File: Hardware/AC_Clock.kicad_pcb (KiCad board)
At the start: 0 parts

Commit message: Set Footprints for components
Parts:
- added C1: 10u, Capacitor_SMD:C_0603_1608Metric, F.Cu at (223.5, 124.5)
- added C2: 22u, Capacitor_SMD:C_0603_1608Metric, F.Cu at (223.5, 127.0)
- added C3: 0.1u, Capacitor_SMD:C_0603_1608Metric, F.Cu at (223.5, 129.5)
- added C4: 0.1u, Capacitor_SMD:C_0603_1608Metric, F.Cu at (223.5, 132.1)
- added C5: 0.1u, Capacitor_SMD:C_0603_1608Metric, F.Cu at (223.5, 134.6)
- added C6: 0.1u, Capacitor_SMD:C_0603_1608Metric, F.Cu at (172.8, 56.0)
- added C7: 0.1u, Capacitor_SMD:C_0603_1608Metric, F.Cu at (172.8, 58.5)
- added C8: 0.1u, Capacitor_SMD:C_0603_1608Metric, F.Cu at (172.8, 61.0)
- added C9: 0.1u, Capacitor_SMD:C_0603_1608Metric, F.Cu at (172.8, 63.5)
- added D1: ABS2, Diode_SMD:Diode_Bridge_Diotec_ABS, F.Cu at (87.6, 124.5)
- added D10: 1N4148WT, Diode_SMD:D_SOD-523, F.Cu at (216.2, 129.4)
- added D11: 1N4148WT, Diode_SMD:D_SOD-523, F.Cu at (216.2, 131.8)
- added D12: 1N4148WT, Diode_SMD:D_SOD-523, F.Cu at (216.2, 134.3)
- added D13: 1N4148WT, Diode_SMD:D_SOD-523, F.Cu at (216.2, 136.7)
- added D14: 1N4148WT, Diode_SMD:D_SOD-523, F.Cu at (219.7, 124.5)
- added D15: 1N4148WT, Diode_SMD:D_SOD-523, F.Cu at (219.7, 126.9)
- added D16: 1N4148WT, Diode_SMD:D_SOD-523, F.Cu at (219.7, 129.4)
- added D17: 1N4148WT, Diode_SMD:D_SOD-523, F.Cu at (219.7, 131.8)
- added D18: 1N4148WT, Diode_SMD:D_SOD-523, F.Cu at (219.7, 134.3)
- added D2: 1N4148WT, Diode_SMD:D_SOD-523, F.Cu at (212.6, 124.5)
- added D3: 1N4148WT, Diode_SMD:D_SOD-523, F.Cu at (212.6, 126.9)
- added D4: 1N4148WT, Diode_SMD:D_SOD-523, F.Cu at (212.6, 129.4)
- added D5: 1N4148WT, Diode_SMD:D_SOD-523, F.Cu at (212.6, 131.8)
- added D6: 1N4148WT, Diode_SMD:D_SOD-523, F.Cu at (212.6, 134.3)
- added D7: 1N4148WT, Diode_SMD:D_SOD-523, F.Cu at (212.6, 136.7)
- added D8: 1N4148WT, Diode_SMD:D_SOD-523, F.Cu at (216.2, 124.5)
- added D9: 1N4148WT, Diode_SMD:D_SOD-523, F.Cu at (216.2, 126.9)
- added F1: LVR005NS, Fuse:Fuse_BelFuse_0ZRE0005FF_L8.3mm_W3.8mm, F.Cu at (38.9, 119.3)
- added J1: L, JKC_Library:Keystone_1287, F.Cu at (38.1, 113.0)
- added J2: N, JKC_Library:Keystone_1287, F.Cu at (38.1, 141.0)
- added JP1: Freq Sel., Jumper:SolderJumper-3_P1.3mm_Bridged12_RoundedPad1.0x1.5mm, F.Cu at (213.6, 139.7)
- added R1: 1k, Resistor_SMD:R_0805_2012Metric, F.Cu at (87.6, 119.5)
- added R10: 1k, Resistor_SMD:R_0805_2012Metric, F.Cu at (221.5, 111.2)
- added R2: 1k, Resistor_SMD:R_0805_2012Metric, F.Cu at (212.6, 105.3)
- added R3: 1k, Resistor_SMD:R_0805_2012Metric, F.Cu at (212.6, 108.3)
- added R4: 1k, Resistor_SMD:R_0805_2012Metric, F.Cu at (212.6, 111.2)
- added R5: 1k, Resistor_SMD:R_0805_2012Metric, F.Cu at (217.1, 105.3)
- added R6: 1k, Resistor_SMD:R_0805_2012Metric, F.Cu at (217.1, 108.3)
- added R7: 1k, Resistor_SMD:R_0805_2012Metric, F.Cu at (217.1, 111.2)
- added R8: 1k, Resistor_SMD:R_0805_2012Metric, F.Cu at (221.5, 105.3)
- added R9: 1k, Resistor_SMD:R_0805_2012Metric, F.Cu at (221.5, 108.3)
- added RN1: 1k, Resistor_SMD:R_Array_Convex_4x0603, F.Cu at (172.9, 47.6)
- added RN2: 1k, Resistor_SMD:R_Array_Convex_4x0603, F.Cu at (177.0, 47.6)
- added RN3: 1k, Resistor_SMD:R_Array_Convex_4x0603, F.Cu at (181.2, 47.6)
- added RN4: 1k, Resistor_SMD:R_Array_Convex_4x0603, F.Cu at (185.3, 47.6)
- added RN5: 1k, Resistor_SMD:R_Array_Convex_4x0603, F.Cu at (189.5, 47.6)
- added RN6: 1k, Resistor_SMD:R_Array_Convex_4x0603, F.Cu at (172.9, 52.4)
- added RN7: 1k, Resistor_SMD:R_Array_Convex_4x0603, F.Cu at (177.0, 52.4)
- added RN8: 1k, Resistor_SMD:R_Array_Convex_4x0603, F.Cu at (181.2, 52.4)
- added RV1: V180ZA, Varistor:RV_Disc_D7mm_W5.1mm_P5mm, F.Cu at (36.9, 134.7)
- added SW1: SW_Push, Button_Switch_SMD:SW_SPST_PTS645, F.Cu at (194.3, 127.2)
- added SW2: SW_Push, Button_Switch_SMD:SW_SPST_PTS645, F.Cu at (194.3, 135.0)
- added T1: 10:1, JKC_Library:Transformer_CL2-5.0R-12, F.Cu at (63.5, 127.0)
- added U1: AZ1117-5.0, Package_TO_SOT_SMD:SOT-223-3_TabPin2, F.Cu at (215.4, 116.9)
- added U10: 4511, Package_SO:TSSOP-16_4.4x5mm_P0.65mm, F.Cu at (166.4, 61.7)
- added U11: HDSP-816E, JKC_Library:Broadcom_HDSP-81x, F.Cu at (216.4, 30.5)
- added U12: 4511, Package_SO:TSSOP-16_4.4x5mm_P0.65mm, F.Cu at (166.4, 68.3)
- added U13: HDSP-816E, JKC_Library:Broadcom_HDSP-81x, F.Cu at (238.2, 30.5)
- added U2: LTV-817S, Package_DIP:SMDIP-6_W9.53mm_Clearance8mm, F.Cu at (90.2, 113.0)
- added U3: 4040, Package_DIP:DIP-16_W7.62mm, F.Cu at (106.7, 119.4)
- added U4: 74LS393, Package_DIP:DIP-14_W7.62mm, F.Cu at (121.9, 130.8)
- added U5: 74LS393, Package_DIP:DIP-14_W7.62mm, F.Cu at (147.3, 130.8)
- added U6: 4511, Package_SO:TSSOP-16_4.4x5mm_P0.65mm, F.Cu at (166.4, 48.5)
- added U7: HDSP-816E, JKC_Library:Broadcom_HDSP-81x, F.Cu at (172.7, 30.5)
- added U8: 4511, Package_SO:TSSOP-16_4.4x5mm_P0.65mm, F.Cu at (166.4, 55.1)
- added U9: HDSP-816E, JKC_Library:Broadcom_HDSP-81x, F.Cu at (194.5, 30.5)
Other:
- copper layers 0 -> 2

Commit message: Work on routing
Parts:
- removed D12: 1N4148WT, Diode_SMD:D_SOD-523
- removed R8: 1k, Resistor_SMD:R_0805_2012Metric
- R1, R10, R2, R3, R4, R5, R6, R7, R9: footprint Resistor_SMD:R_0805_2012Metric -> Resistor_SMD:R_0603_1608Metric
- SW1: value SW_Push -> Min_PB
- SW2: value SW_Push -> Hr_PB
- U11, U13, U7, U9: moved to B.Cu
- moved C1 137.9 mm to (85.9, 132.1)
- moved C2 133.9 mm to (89.7, 132.1)
- moved U1 129.5 mm to (87.6, 138.4), turned to -90 degrees
- moved C3 126.1 mm to (97.8, 139.7), turned to -90 degrees
- moved R2 119.5 mm to (94.0, 119.8), turned to 90 degrees
- moved R3 117.5 mm to (95.2, 113.0), turned to -90 degrees
- moved D4 115.9 mm to (97.8, 113.0), turned to 90 degrees
- moved C4 113.3 mm to (110.5, 124.5), turned to -90 degrees
- moved D3 113.1 mm to (100.3, 113.0), turned to 90 degrees
- moved D2 110.3 mm to (102.9, 113.0), turned to 90 degrees
- moved D5 108.8 mm to (105.4, 113.0), turned to 90 degrees
- moved JP1 105.6 mm to (108.0, 142.2), turned to 180 degrees
- moved D15 104.5 mm to (115.6, 134.6), turned to -90 degrees
- moved R9 104.2 mm to (120.7, 134.6), turned to 90 degrees
- moved D16 101.8 mm to (118.1, 134.6), turned to -90 degrees
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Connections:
- net Net-(D16-A) renamed /SetM
- net Net-(D18-A) renamed /SetH
- net Net-(D3-K) renamed /16s
- net Net-(D4-K) renamed /8s
- net Net-(F1-Pad2) renamed /Fused
- D14 pad 2: /RST_{10hr} -> DA_4
- D2 pad 1: /minute -> /32s
- D2 pad 2: Net-(D2-A) -> /minute
- D3 pad 2: Net-(D2-A) -> /minute
- D4 pad 2: Net-(D2-A) -> /minute
- D5 pad 2: Net-(D2-A) -> /minute
- R3 pad 1: Net-(D2-A) -> /minute
- U3 pad 1: /minute -> /32s
- U3 pad 11: Net-(D2-A) -> /minute
- U5 pad 12: /RST_{10hr} -> DA_4
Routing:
- net +5V: track 0.00 -> 143.3 mm, vias 0 -> 2
- net /AC_12+: track 0.00 -> 50.8 mm
- net Earth: track 0.00 -> 50.4 mm
- net /minute: track 0.00 -> 45.7 mm, vias 0 -> 1
- net Net-(JP1-C): track 0.00 -> 41.8 mm
- net /Fused: track 0.00 -> 40.0 mm
- net /10hr: track 0.00 -> 27.7 mm
- net GND: track 0.00 -> 24.9 mm, vias 0 -> 10
- net /32s: track 0.00 -> 23.2 mm
- net /10m: track 0.00 -> 22.7 mm
- net /16s: track 0.00 -> 20.7 mm
- net /8s: track 0.00 -> 18.5 mm
- net AC: track 0.00 -> 17.2 mm
- net /AC_12-: track 0.00 -> 14.7 mm
- net DA_4: track 0.00 -> 14.2 mm
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- added copper zone on B.Cu, net Earth
- added copper zone on B.Cu, net GND
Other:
- board outline added: 127 x 40.6 mm

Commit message: Add in correct calculated times for frequency divider
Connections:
- net /16s renamed /17s
- net /32s renamed /34s
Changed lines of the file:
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@@
 	(net 111 "unconnected-(RN8-R4.1-Pad4)")
 	(net 112 "unconnected-(RN8-R4.2-Pad5)")
-	(net 113 "/32s")
-	(net 114 "/16s")
+	(net 113 "/34s")
+	(net 114 "/17s")
 	(net 115 "/8s")
 	(net 116 "/Fused")
@@
 			(layers "F.Cu" "F.Paste" "F.Mask")
 			(roundrect_rratio 0.25)
-			(net 114 "/16s")
+			(net 114 "/17s")
 			(pinfunction "K")
 			(pintype "passive")
@@
 			(layers "F.Cu" "F.Paste" "F.Mask")
 			(roundrect_rratio 0.25)
-			(net 113 "/32s")
+			(net 113 "/34s")
 			(pinfunction "K")
 			(pintype "passive")
@@
 		)
 		(fp_text user "${REFERENCE}"
-			(at 0 0 360)
+			(at 0 0 0)
 			(layer "F.Fab")
 			(effects
@@
 		(tags "net tie solder jumper bridged")
 		(property "Reference" "JP1"
-			(at 0 -1.8 360)
+			(at 0 -1.8 0)
 			(layer "F.SilkS")
 			(effects
@@
 		)
 		(property "Value" "Freq Sel."
-			(at 0 1.9 360)
+			(at 0 1.9 0)
 			(layer "F.Fab")
 			(effects
@@
 		(tags "SPST Button Switch")
 		(property "Reference" "SW2"
-			(at 0 -4.05 360)
+			(at 0 -4.05 0)
 			(layer "F.SilkS")
 			(hide yes)
@@
 		)
 		(property "Value" "Hr_PB"
-			(at 0 -5.08 360)
+			(at 0 -5.08 0)
 			(layer "F.SilkS")
 			(effects
@@
 		)
 		(fp_text user "${REFERENCE}"
-			(at 0 -4.05 360)
+			(at 0 -4.05 0)
 			(layer "F.Fab")
 			(effects
@@
 		(tags "SPST Button Switch")
 		(property "Reference" "SW1"
-			(at 0 -4.05 360)
+			(at 0 -4.05 0)
 			(layer "F.SilkS")
 			(hide yes)
@@
 		)
 		(property "Value" "Min_PB"
-			(at 0 -5.08 360)
+			(at 0 -5.08 0)
 			(layer "F.SilkS")
 			(effects
@@
 		)
 		(fp_text user "${REFERENCE}"
-			(at 0 -4.05 360)
+			(at 0 -4.05 0)
 			(layer "F.Fab")
 			(effects
@@
 		(tags "THT DIP DIL PDIP 2.54mm 7.62mm 300mil")
 		(property "Reference" "U3"
-			(at 3.81 -2.33 360)
+			(at 3.81 -2.33 0)
 			(layer "F.SilkS")
 			(effects
@@
 		)
 		(property "Value" "4040"
-			(at 3.81 20.11 360)
+			(at 3.81 20.11 0)
 			(layer "F.Fab")
 			(effects
@@
 		)
 		(fp_text user "${REFERENCE}"
-			(at 3.81 8.89 360)
+			(at 3.81 8.89 0)
 			(layer "F.Fab")
 			(effects
@@
 			(layers "*.Cu" "*.Mask")
 			(remove_unused_layers no)
-			(net 113 "/32s")
+			(net 113 "/34s")
 			(pinfunction "Q11")
 			(pintype "output")
@@
 			(layers "*.Cu" "*.Mask")
 			(remove_unused_layers no)
-			(net 114 "/16s")
+			(net 114 "/17s")
 			(pinfunction "Q10")
 			(pintype "output")
@@
 		)
 		(fp_text user "${REFERENCE}"
-			(at -1.27 -11.43 360)
+			(at -1.27 -11.43 0)
 			(layer "B.Fab")
 			(effects
@@
 		)
 		(fp_text user "${REFERENCE}"
-			(at -1.27 -11.43 360)
+			(at -1.27 -11.43 0)
 			(layer "B.Fab")
 			(effects
@@
 		)
 		(fp_text user "${REFERENCE}"
-			(at -1.27 -11.43 360)
+			(at -1.27 -11.43 0)
 			(layer "B.Fab")
 			(effects
@@
 		)
 		(fp_text user "${REFERENCE}"
-			(at -1.27 -11.43 360)
+			(at -1.27 -11.43 0)
 			(layer "B.Fab")
 			(effects

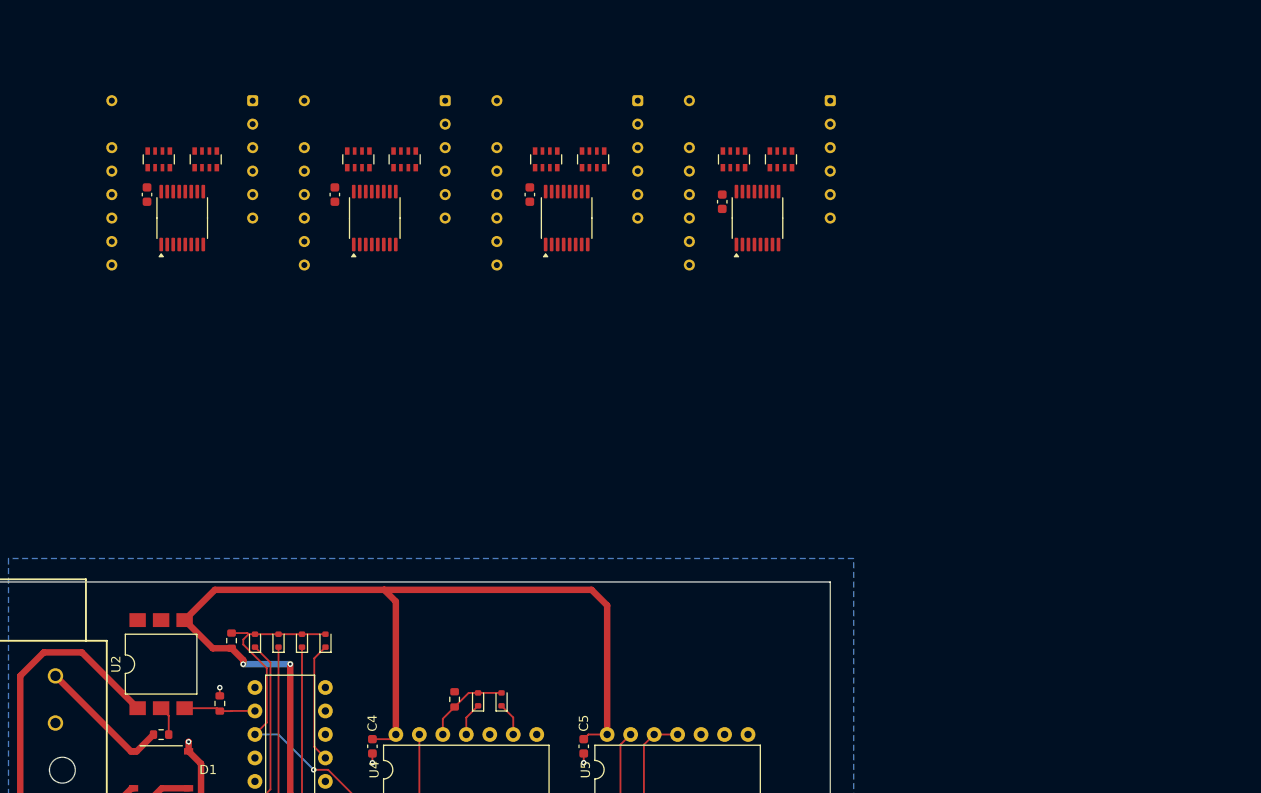
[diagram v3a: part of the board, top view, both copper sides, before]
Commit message: Add in connectors for display board interconnect
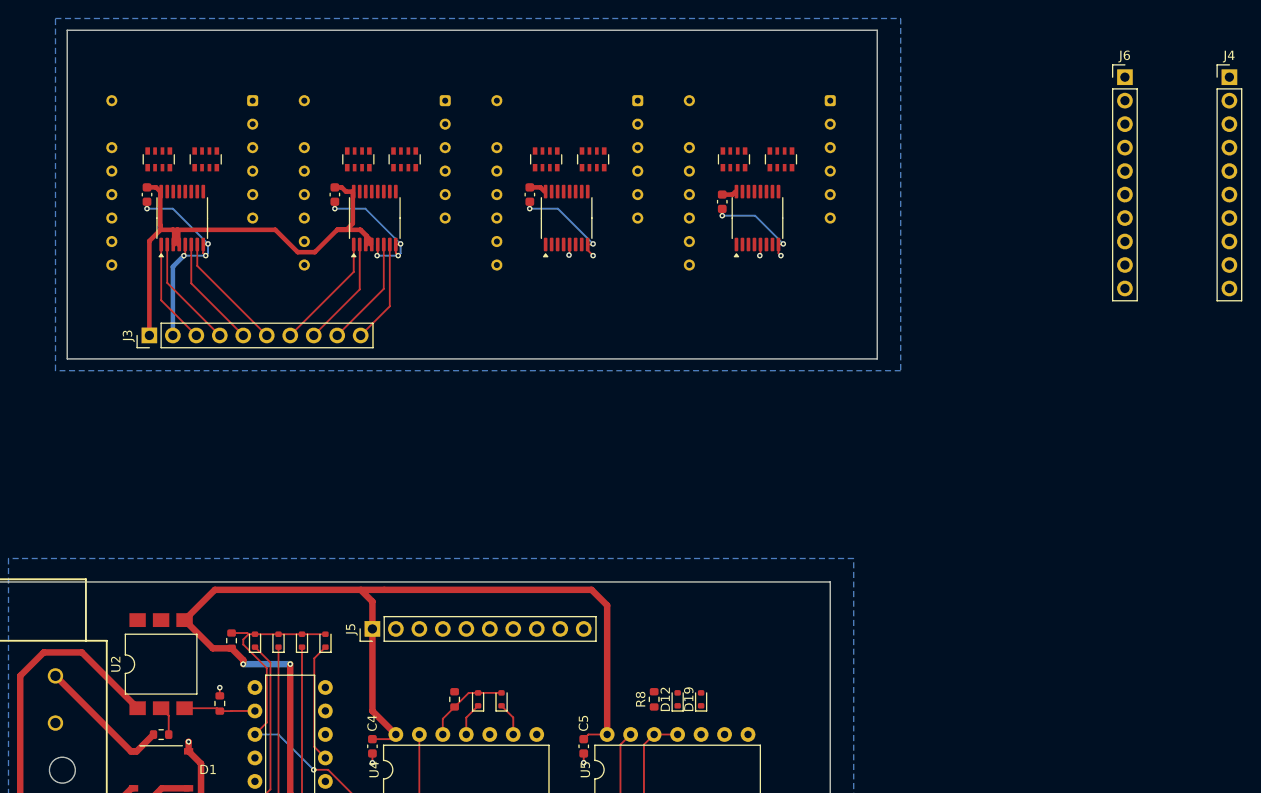
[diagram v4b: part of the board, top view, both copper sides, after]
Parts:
- added D12: 1N4148WT, Diode_SMD:D_SOD-523, F.Cu at (143.5, 119.4)
- added D19: 1N4148WT, Diode_SMD:D_SOD-523, F.Cu at (146.1, 119.4)
- added J3: Conn_01x10, Connector_PinHeader_2.54mm:PinHeader_1x10_P2.54mm_Vertical, F.Cu at (86.4, 80.0)
- added J4: Conn_01x10, Connector_PinHeader_2.54mm:PinHeader_1x10_P2.54mm_Vertical, F.Cu at (203.2, 52.1)
- added J5: Conn_01x10, Connector_PinHeader_2.54mm:PinHeader_1x10_P2.54mm_Vertical, F.Cu at (110.5, 111.8)
- added J6: Conn_01x10, Connector_PinHeader_2.54mm:PinHeader_1x10_P2.54mm_Vertical, F.Cu at (191.9, 52.1)
- added R8: 1k, Resistor_SMD:R_0603_1608Metric, F.Cu at (141.0, 119.4)
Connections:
- D11 pad 1: DA_3 -> DB_3
- D14 pad 2: DA_4 -> /RST_{10hr}
- D7 pad 1: DA_1 -> DB_1
- D9 pad 1: DA_2 -> DB_2
- U5 pad 12: DA_4 -> /RST_{10hr}
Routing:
- net GND: track 24.9 -> 90.1 mm, vias 10 -> 26
- net +5V: track 143.3 -> 203.8 mm
- net DA_1: track 6.38 -> 19.3 mm
- net DB_2: track 0.00 -> 12.7 mm
- net DC_1: track 0.00 -> 12.2 mm
- net DD_1: track 3.12 -> 15.3 mm
- net DD_2: track 0.00 -> 11.9 mm
- net DC_2: track 3.62 -> 15.5 mm
- net DB_1: track 0.00 -> 11.4 mm
- net DA_2: track 3.63 -> 14.8 mm
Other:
- board size 127 x 40.6 mm -> 132.1 x 100.3 mm

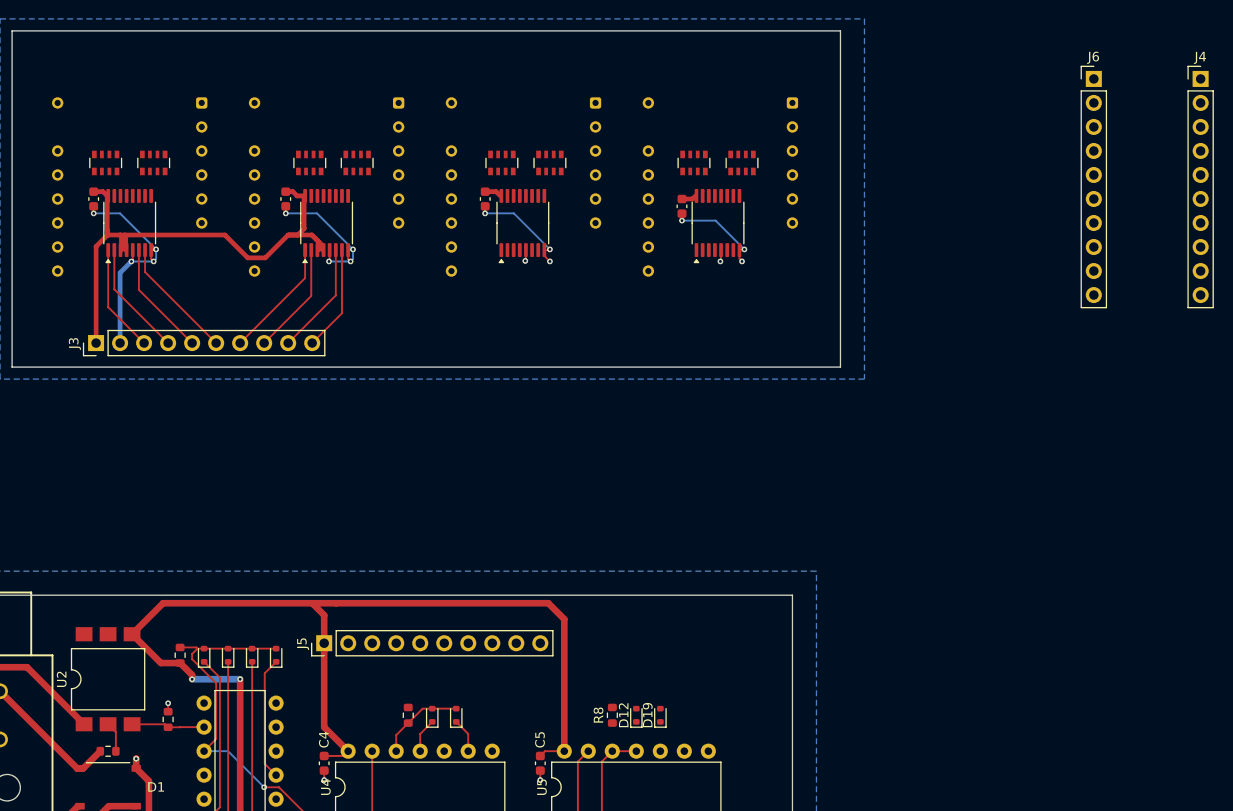
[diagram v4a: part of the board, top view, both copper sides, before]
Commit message: Adjust minutes resistor packs to make them flow better
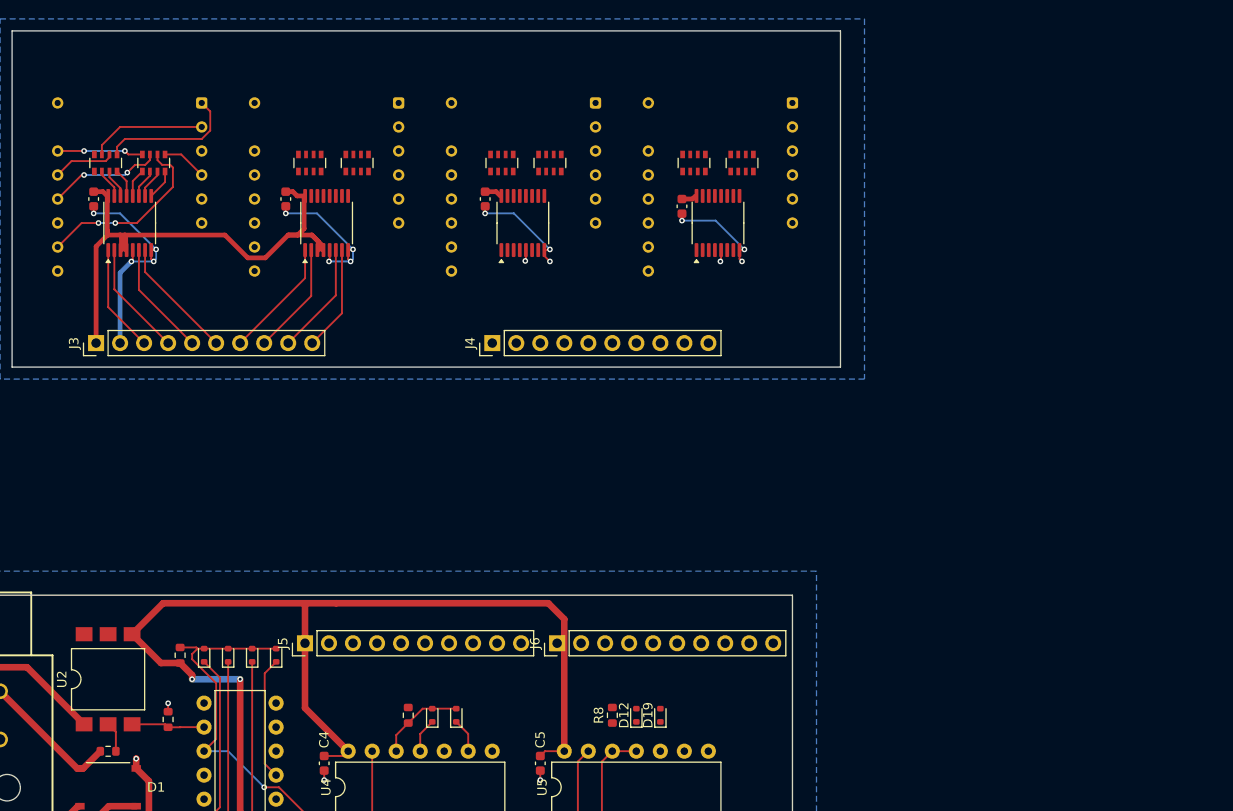
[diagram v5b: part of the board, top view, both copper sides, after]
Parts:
- moved J6 82.4 mm to (135.1, 111.8), turned to 90 degrees
- moved J4 80.0 mm to (128.3, 80.0), turned to 90 degrees
- moved J5 2.03 mm to (108.5, 111.8)
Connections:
- RN2 pad 1: Net-(RN2-R1.1) -> unconnected-(RN2A-R1.1-Pad1)
- RN2 pad 4: unconnected-(RN2-R4.1-Pad4) -> Net-(RN2D-R4.1)
- RN2 pad 5: unconnected-(RN2-R4.2-Pad5) -> Net-(RN2D-R4.2)
- RN2 pad 8: Net-(RN2-R1.2) -> unconnected-(RN2A-R1.2-Pad8)
- RN3 pad 1: Net-(RN3-R1.1) -> unconnected-(RN3A-R1.1-Pad1)
- RN3 pad 2: Net-(RN3-R2.1) -> Net-(RN3B-R2.1)
- RN3 pad 3: Net-(RN3-R3.1) -> Net-(RN3C-R3.1)
- RN3 pad 4: Net-(RN3-R4.1) -> Net-(RN3D-R4.1)
- RN3 pad 5: Net-(RN3-R4.2) -> Net-(RN3D-R4.2)
- RN3 pad 6: Net-(RN3-R3.2) -> Net-(RN3C-R3.2)
- RN3 pad 7: Net-(RN3-R2.2) -> Net-(RN3B-R2.2)
- RN3 pad 8: Net-(RN3-R1.2) -> unconnected-(RN3A-R1.2-Pad8)
- RN4 pad 4: unconnected-(RN4-R4.1-Pad4) -> Net-(RN4-R4.1)
- RN4 pad 5: unconnected-(RN4-R4.2-Pad5) -> Net-(RN4-R4.2)
- U6 pad 10: Net-(RN1-R4.1) -> Net-(RN1-R3.1)
- U6 pad 11: Net-(RN1-R3.1) -> Net-(RN1-R2.1)
- U6 pad 12: Net-(RN1-R2.1) -> Net-(RN1-R1.1)
- U6 pad 13: Net-(RN1-R1.1) -> Net-(RN2D-R4.1)
- U6 pad 9: Net-(RN2-R1.1) -> Net-(RN1-R4.1)
- U7 pad 1: Net-(RN1-R1.2) -> Net-(RN2D-R4.2)
- U7 pad 10: Net-(RN1-R4.2) -> Net-(RN1-R3.2)
- U7 pad 12: Net-(RN1-R3.2) -> Net-(RN1-R2.2)
- U7 pad 14: Net-(RN1-R2.2) -> Net-(RN1-R1.2)
- U7 pad 4: Net-(RN2-R1.2) -> Net-(RN1-R4.2)
- U8 pad 10: Net-(RN3-R4.1) -> Net-(RN4-R3.1)
- U8 pad 11: Net-(RN3-R3.1) -> Net-(RN4-R2.1)
- U8 pad 12: Net-(RN3-R2.1) -> Net-(RN4-R1.1)
- U8 pad 13: Net-(RN3-R1.1) -> Net-(RN3D-R4.1)
- U8 pad 14: Net-(RN4-R3.1) -> Net-(RN3C-R3.1)
- U8 pad 15: Net-(RN4-R2.1) -> Net-(RN3B-R2.1)
- U8 pad 9: Net-(RN4-R1.1) -> Net-(RN4-R4.1)
- U9 pad 1: Net-(RN3-R1.2) -> Net-(RN3D-R4.2)
- U9 pad 10: Net-(RN3-R4.2) -> Net-(RN4-R3.2)
- U9 pad 12: Net-(RN3-R3.2) -> Net-(RN4-R2.2)
- U9 pad 13: Net-(RN4-R3.2) -> Net-(RN3C-R3.2)
- U9 pad 14: Net-(RN3-R2.2) -> Net-(RN4-R1.2)
- U9 pad 2: Net-(RN4-R2.2) -> Net-(RN3B-R2.2)
- U9 pad 4: Net-(RN4-R1.2) -> Net-(RN4-R4.2)
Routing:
- net Net-(RN1-R3.2): track 0.00 -> 19.4 mm, vias 0 -> 2
- net Net-(RN2D-R4.2): track 0.00 -> 14.7 mm
- net Net-(RN2B-R2.2): track 0.00 -> 12.3 mm
- net Net-(RN1-R2.2): track 0.00 -> 12.1 mm, vias 0 -> 2
- net Net-(RN1-R1.2): track 0.00 -> 9.11 mm, vias 0 -> 2
- net Net-(RN2C-R3.2): track 0.00 -> 6.55 mm
- net Net-(RN1-R4.2): track 0.00 -> 4.78 mm
- net Net-(RN1-R4.1): track 0.00 -> 3.19 mm
- net Net-(RN2B-R2.1): track 0.00 -> 3.13 mm
- net Net-(RN1-R3.1): track 0.00 -> 3.13 mm
- net Net-(RN2C-R3.1): track 0.00 -> 3.07 mm
- net Net-(RN1-R2.1): track 0.00 -> 3.07 mm
- net Net-(RN2D-R4.1): track 0.00 -> 3.01 mm
- net Net-(RN1-R1.1): track 0.00 -> 3.01 mm
